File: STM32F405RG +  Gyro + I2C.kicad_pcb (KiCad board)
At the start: 4 copper layers, 62 parts, among them J1 USB_B_Micro, J2 USART_CONN, J3 SWD_CONN, J4 12V_CONN, Q1 AO3401A, SW1 SW_SPDT, U1 MP2359DJ-LF-Z, U2 MPU-6000, U3 USBLC6-2SC6, U4 STM32F405RGTx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

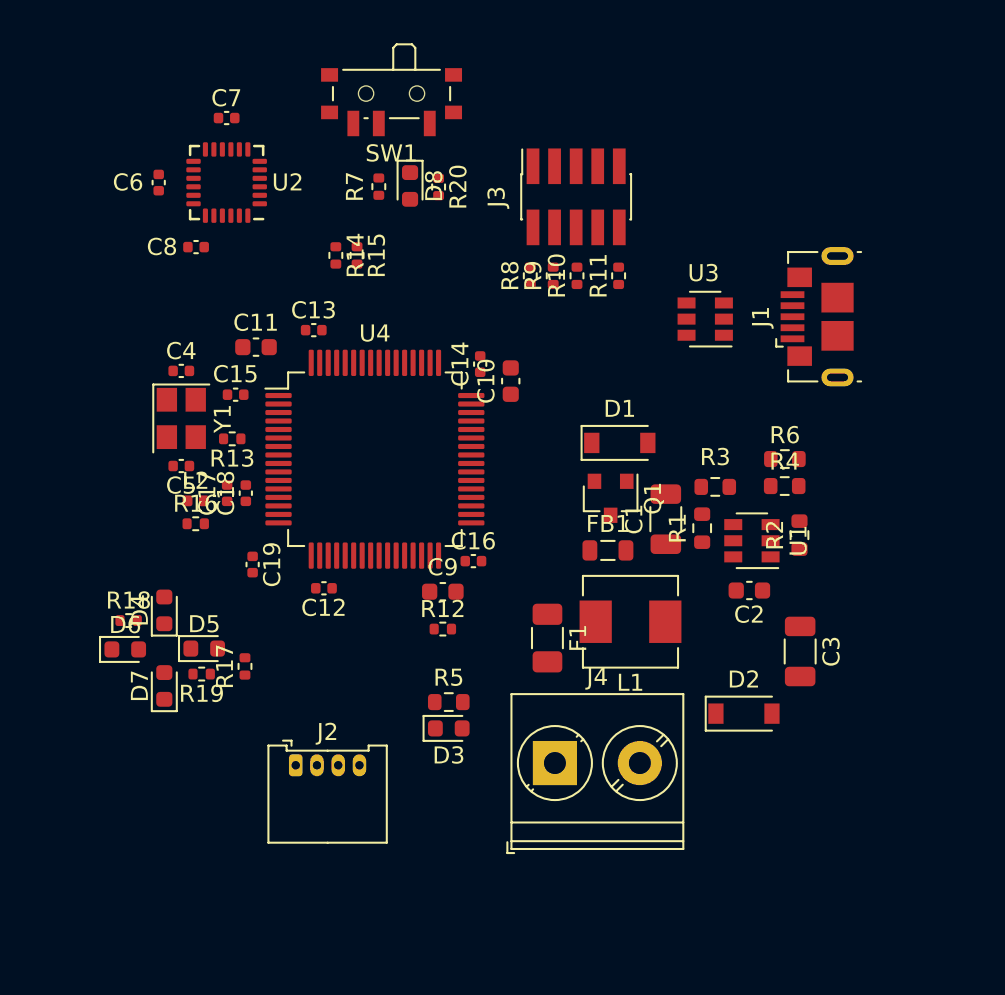
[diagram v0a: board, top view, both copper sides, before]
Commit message: Changed power supply layout
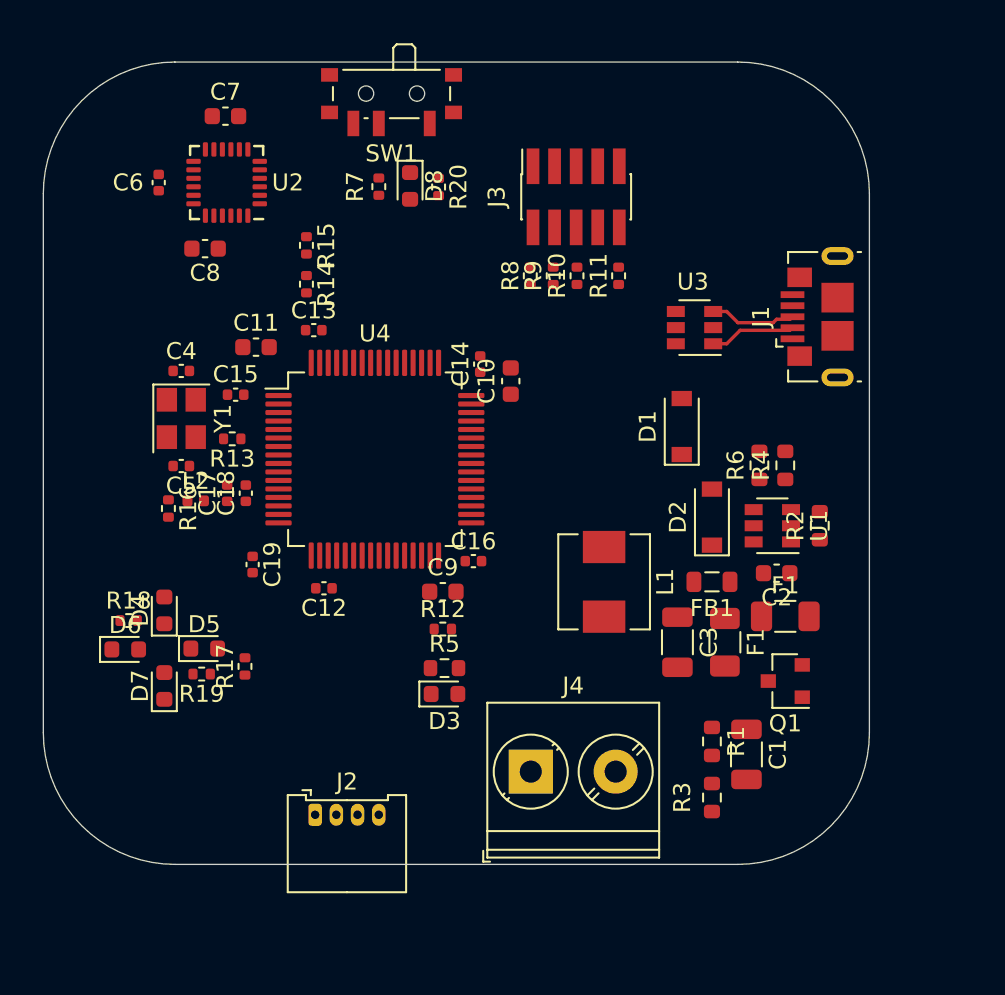
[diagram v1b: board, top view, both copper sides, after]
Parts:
- removed the F1 at (155.2, 112.5)
- added F1: 250mA, Fuse:Fuse_1206_3216Metric, F.Cu at (169.2, 111.3)
- added F1: 250mA, Fuse:Fuse_1206_3216Metric, F.Cu at (165.6, 112.8)
- C7, C8: footprint Capacitor_SMD:C_0402_1005Metric -> Capacitor_SMD:C_0603_1608Metric
- moved R3 18.3 mm to (164.8, 121.9), turned to 270 degrees
- moved Q1 14.9 mm to (169.2, 115.1), turned to 180 degrees
- moved C1 14.6 mm to (166.9, 119.4), turned to 270 degrees
- moved R1 12.6 mm to (164.8, 118.6), turned to 270 degrees
- moved D2 11.7 mm to (164.8, 105.4), turned to 90 degrees
- moved C3 7.25 mm to (162.8, 112.8)
- moved FB1 6.40 mm to (164.8, 109.2), turned to 180 degrees
- moved D1 3.77 mm to (163.1, 100.1), turned to 90 degrees
- moved J2 3.13 mm to (141.5, 122.9)
- moved R15 3.04 mm to (141.0, 89.4)
- moved L1 2.82 mm to (158.5, 109.2), turned to 270 degrees
- moved R14 2.42 mm to (141.0, 91.7)
- moved D3 2.04 mm to (149.1, 115.8)
- moved R5 2.02 mm to (149.1, 114.3)
- moved C2 1.90 mm to (168.7, 108.7)
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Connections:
- FB1 pad 1: Net-(D1-Pad1) -> Net-(F1-Pad1)
- Q1 pad 3: Net-(F1-Pad1) -> +12V
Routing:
- net USB_CONN_D+: track 0.00 -> 5.09 mm
- net USB_CONN_D-: track 0.00 -> 5.06 mm
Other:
- board outline added: 48.6 x 47.2 mm

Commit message: Changes & PCB routing
Changed pin on LED, started routing signals and differential pairs
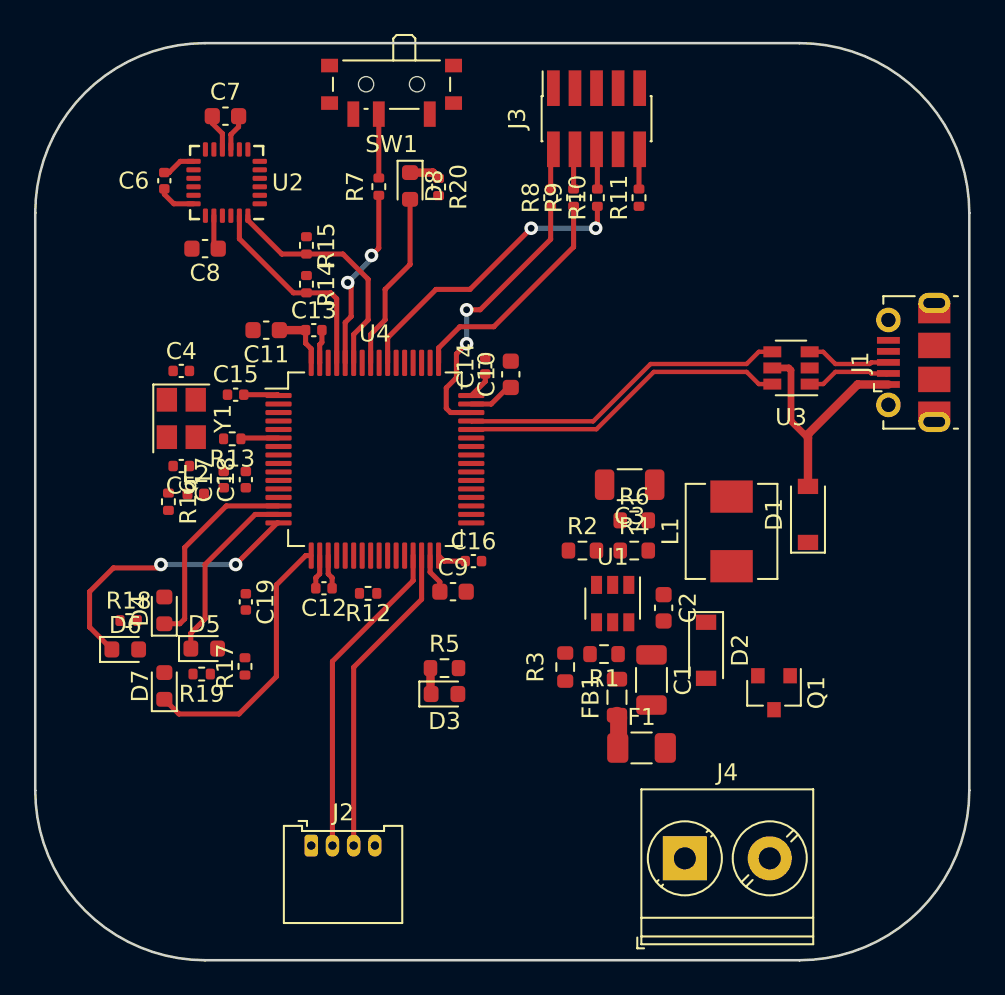
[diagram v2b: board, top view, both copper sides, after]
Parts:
- removed the F1 at (169.2, 111.3)
- J1: footprint USB Footprint Library:USB_Micro-B_GCT_USB3076-30-A -> USB Footprint Library:USB_Micro-B_Molex-105017-0001
- moved R2 14.1 mm to (157.2, 107.4), turned to 0 degrees
- moved R3 11.6 mm to (156.2, 114.2)
- moved U1 10.5 mm to (159.0, 110.5), turned to 270 degrees
- moved J4 10.4 mm to (163.2, 125.5)
- moved R4 10.2 mm to (160.3, 107.4), turned to 0 degrees
- moved C3 9.69 mm to (160.0, 103.5), turned to 180 degrees
- moved D1 9.06 mm to (170.5, 105.2)
- moved FB1 8.80 mm to (159.3, 116.0), turned to 90 degrees
- moved R1 8.18 mm to (158.5, 113.5), turned to 180 degrees
- moved L1 8.07 mm to (166.0, 106.2), turned to 90 degrees
- moved R6 8.05 mm to (160.3, 105.6), turned to 180 degrees
- moved F1 7.93 mm to (160.7, 119.0), turned to 0 degrees
- moved D2 7.85 mm to (164.5, 113.2), turned to 270 degrees
- moved C1 7.10 mm to (161.3, 115.0)
- moved C2 6.96 mm to (162.0, 110.8), turned to 270 degrees
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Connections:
- U4 pad 53: LED -> Net-(U4-Pad53)
- U4 pad 57: Net-(U4-Pad57) -> LED
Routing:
- net USB_OTG_FS_D-: track 0.00 -> 19.4 mm
- net USB_OTG_FS_D+: track 0.00 -> 19.4 mm
- net USART_TX: track 0.00 -> 19.0 mm
- net USART_RX: track 0.00 -> 18.7 mm
- net SWO: track 0.00 -> 17.7 mm, vias 0 -> 2
- net TIM2_CH3: track 0.00 -> 16.7 mm, vias 0 -> 2
- net SWDIO: track 0.00 -> 16.5 mm, vias 0 -> 2
- net TIM2_CH4: track 0.00 -> 16.0 mm
- net +5V: track 0.00 -> 14.6 mm
- net I2C_SDA: track 0.00 -> 14.1 mm
- net SWCLK: track 0.00 -> 13.7 mm
- net +3V3: track 0.00 -> 13.0 mm
- net I2C_SCL: track 0.00 -> 12.3 mm
- net TIM2_CH1: track 0.00 -> 12.1 mm
- net BOOT0: track 0.00 -> 10.9 mm, vias 0 -> 2
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- added copper zone on In2.Cu, net +3V3
- added copper zone on In1.Cu, net GND
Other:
- board size 48.6 x 47.2 mm -> 55 x 54 mm

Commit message: Fixed layout and added text to silkscreen
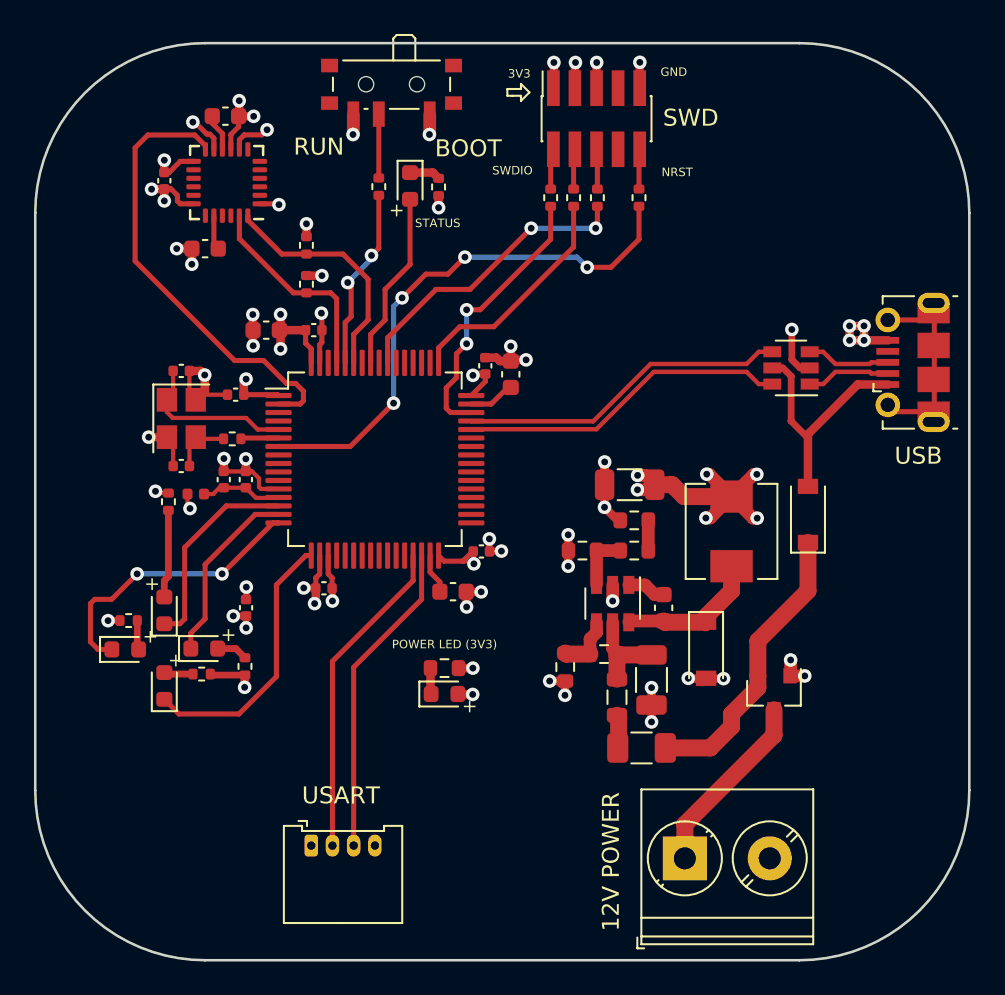
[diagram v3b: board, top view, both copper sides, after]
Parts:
- removed R12: 10k, Resistor_SMD:R_0402_1005Metric
- moved C16 0.74 mm to (151.3, 107.4)
- moved C19 0.34 mm to (137.4, 110.7)
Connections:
- U4 pad 2: Net-(U4-Pad2) -> GYRO_INT
- U4 pad 24: GYRO_INT -> Net-(U4-Pad24)
- U4 pad 28: BOOT1 -> Net-(U4-Pad28)
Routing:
- net GND: track 8.42 -> 73.5 mm, vias 0 -> 47
- net +3V3: track 13.0 -> 50.7 mm, vias 0 -> 26
- net NRST: track 0.00 -> 32.1 mm, vias 0 -> 4
- net GYRO_INT: track 0.00 -> 26.8 mm
- net Net-(D1-Pad1): track 0.00 -> 17.1 mm
- net Net-(J1-Pad6): track 0.00 -> 13.9 mm
- net +12V: track 0.00 -> 10.9 mm
- net HSE_IN: track 0.00 -> 9.58 mm
- net Net-(C2-Pad2): track 0.00 -> 8.53 mm
- net BUCK_IN: track 0.00 -> 5.50 mm
- net Net-(D4-Pad2): track 0.00 -> 5.20 mm
- net +3.3VA: track 0.00 -> 4.81 mm
- net Net-(C5-Pad1): track 0.00 -> 3.53 mm
- net Net-(R1-Pad2): track 0.00 -> 3.52 mm
- net BUCK_FB: track 0.00 -> 3.42 mm
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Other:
- rule trace_min: 0.2 -> 0.25
- board text added: "+"
- board text added: "12V POWER"
- board text added: "3V3"
- board text added: "BOOT"
- board text added: "GND"
- board text added: "NRST"
- board text added: "POWER LED (3V3)"
- board text added: "RUN"
- board text added: "STATUS"
- board text added: "SWD"
- board text added: "SWDIO"
- board text added: "USART"
- board text added: "USB"

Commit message: Changes
FIX: Changed SWD connector from socket to header
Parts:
- J3: footprint Connector_PinSocket_1.27mm:PinSocket_2x05_P1.27mm_Vertical_SMD -> Connector_PinHeader_1.27mm:PinHeader_2x05_P1.27mm_Vertical_SMD
- moved J2 9.18 mm to (150.4, 125.4)
- moved R8 5.43 mm to (160.6, 88.0)
- moved R11 5.25 mm to (155.5, 88.0)
- moved R9 2.97 mm to (159.3, 88.0)
- moved R10 1.44 mm to (158.0, 88.0)
- moved J3 0.59 mm to (158.0, 82.5), turned to 270 degrees
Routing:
- net NRST: track 32.1 -> 25.1 mm, vias 4 -> 2
- net USART_TX: track 19.0 -> 25.7 mm
- net USART_RX: track 18.7 -> 25.4 mm
- net SWDIO: track 16.5 -> 19.7 mm, vias 2 -> 0
- net SWO: track 17.7 -> 16.1 mm, vias 2 -> 0
- net SWCLK: track 13.7 -> 14.9 mm
- net Net-(J3-Pad6): track 2.36 -> 3.04 mm
- net Net-(J3-Pad10): track 2.36 -> 3.03 mm
- net Net-(J3-Pad4): track 2.37 -> 3.04 mm
- net Net-(J3-Pad2): track 2.41 -> 3.04 mm
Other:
- board text added: "-"
- board text added: "STM32F4 + GYRO + I2C"

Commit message: Added BOM file
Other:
- board text added: "JLCJLCJLCJLC"
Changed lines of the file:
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@@
   (general
     (thickness 1.6)
-    (drawings 44)
+    (drawings 45)
     (tracks 504)
     (zones 0)
@@
   )
   (setup
-    (last_trace_width 0.3)
+    (last_trace_width 0.25)
     (user_trace_width 0.3)
     (user_trace_width 0.4)
@@
       (effects (font (size 1 1) (thickness 0.15)))
     )
-    (fp_text user %R (at 0 0 180) (layer F.Fab)
-      (effects (font (size 1 1) (thickness 0.15)))
-    )
     (fp_line (start 1.705 3.175) (end -1.705 3.175) (layer F.Fab) (width 0.1))
     (fp_line (start -1.27 -3.175) (end 1.705 -3.175) (layer F.Fab) (width 0.1))
@@
     (fp_line (start 4.3 3.7) (end 4.3 -3.7) (layer F.CrtYd) (width 0.05))
     (fp_line (start 4.3 -3.7) (end -4.3 -3.7) (layer F.CrtYd) (width 0.05))
+    (fp_text user %R (at 0 0 180) (layer F.Fab)
+      (effects (font (size 1 1) (thickness 0.15)))
+    )
     (pad 10 smd rect (at 1.95 2.54 270) (size 2.4 0.74) (layers F.Cu F.Paste F.Mask)
       (net 39 "Net-(J3-Pad10)"))
@@
     )
   )
+  (gr_text JLCJLCJLCJLC (at 145.034 102.362) (layer F.SilkS)
+    (effects (font (size 0.9 0.9) (thickness 0.15)))
+  )
   (gr_text "STM32F4 + GYRO + I2C" (at 178.054 114.046 90) (layer F.SilkS)
     (effects (font (size 1 1) (thickness 0.25) italic))
@@
   (segment (start 159.31 80.59) (end 159.3 80.58) (width 0.3) (layer F.Cu) (net 2) (status C00000))
   (segment (start 159.3 80.58) (end 159.3 78.95) (width 0.3) (layer F.Cu) (net 2) (status 400000))
-  (via (at 160.61 78.95) (size 0.8) (drill 0.4) (layers F.Cu B.Cu) (net 5))
-  (segment (start 160.58 80.59) (end 160.61 80.56) (width 0.3) (layer F.Cu) (net 5) (status C00000))
-  (segment (start 160.61 80.56) (end 160.61 78.95) (width 0.3) (layer F.Cu) (net 5) (status 400000))
+  (via (at 155.49 78.94) (size 0.8) (drill 0.4) (layers F.Cu B.Cu) (net 2))
+  (segment (start 155.49 80.58) (end 155.5 80.59) (width 0.3) (layer F.Cu) (net 2) (status C00000))
+  (segment (start 155.49 78.94) (end 155.49 80.58) (width 0.3) (layer F.Cu) (net 2) (status 800000))
   (segment (start 162 109.975) (end 161.475 109.975) (width 0.75) (layer F.Cu) (net 3) (status 400000))
   (segment (start 160.9 109.4) (end 159.95 109.4) (width 0.75) (layer F.Cu) (net 3) (status 800000))
@@
   (segment (start 162 111.525) (end 160.025 111.525) (width 0.75) (layer F.Cu) (net 4) (status C00000))
   (segment (start 160.025 111.525) (end 159.95 111.6) (width 0.75) (layer F.Cu) (net 4) (status C00000))
+  (via (at 160.61 78.95) (size 0.8) (drill 0.4) (layers F.Cu B.Cu) (net 5))
+  (segment (start 160.58 80.59) (end 160.61 80.56) (width 0.3) (layer F.Cu) (net 5) (status C00000))
+  (segment (start 160.61 80.56) (end 160.61 78.95) (width 0.3) (layer F.Cu) (net 5) (status 400000))
   (via (at 141.88 91.19) (size 0.8) (drill 0.4) (layers F.Cu B.Cu) (net 5))
   (segment (start 140.97 91.184) (end 140.976 91.19) (width 0.5) (layer F.Cu) (net 5) (status C00000))
@@
   (segment (start 135.37 114.71) (end 135.31 114.65) (width 0.4) (layer F.Cu) (net 5) (status C00000))
   (segment (start 139.275 98.2) (end 139.325 98.25) (width 0.3) (layer F.Cu) (net 5) (status C00000))
-  (via (at 155.49 78.94) (size 0.8) (drill 0.4) (layers F.Cu B.Cu) (net 2))
-  (segment (start 155.49 80.58) (end 155.5 80.59) (width 0.3) (layer F.Cu) (net 2) (status C00000))
-  (segment (start 155.49 78.94) (end 155.49 80.58) (width 0.3) (layer F.Cu) (net 2) (status 800000))
   (segment (start 139.325 100.25) (end 138.096 100.25) (width 0.25) (layer F.Cu) (net 6) (status 400000))
   (segment (start 132.75 99.222) (end 132.75 98.5) (width 0.25) (layer F.Cu) (net 6) (status 800000))

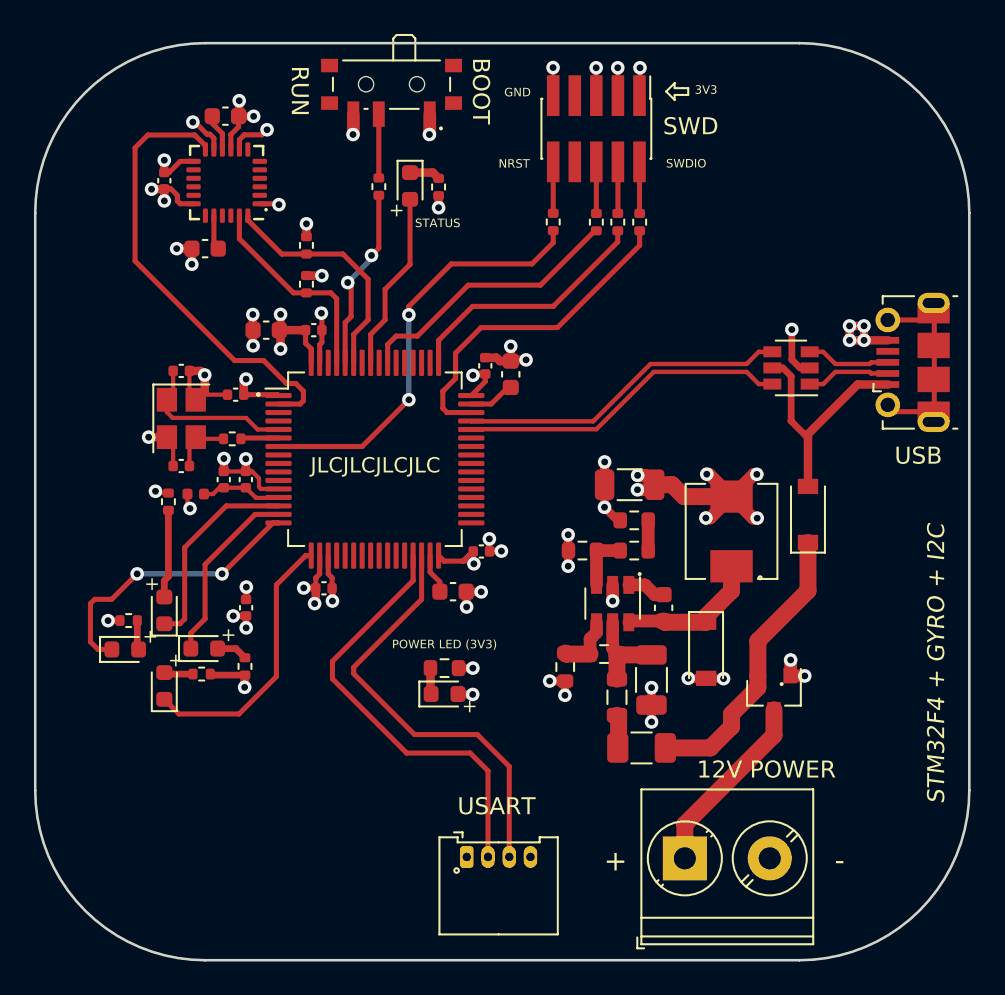
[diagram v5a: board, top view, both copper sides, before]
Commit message: Changed gyroscope, added gerber and assembly files
-Changed Gyroscope from MPU-6000 to MPU-6050
-Added Gerber and Assembly files
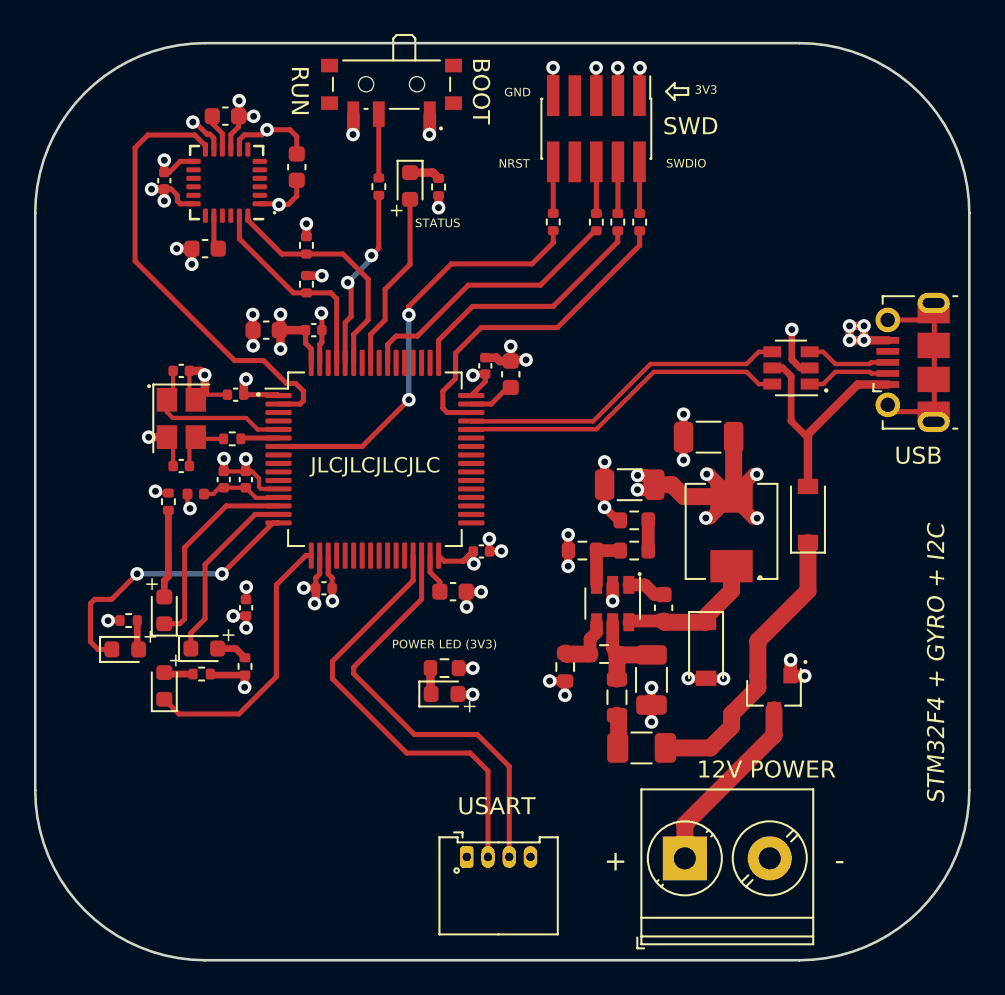
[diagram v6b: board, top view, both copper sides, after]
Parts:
- added C20: 10uF, Capacitor_SMD:C_1206_3216Metric, F.Cu at (164.7, 100.7)
- added C21: 10nF, Capacitor_SMD:C_0603_1608Metric, F.Cu at (140.4, 84.8)
- C3: value 22uF -> 10uF
- R13: value 68 -> 47
- U2: value MPU-6000 -> MPU-6050
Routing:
- net +3V3: track 50.8 -> 57.3 mm
- net GND: track 73.8 -> 78.7 mm, vias 47 -> 49
